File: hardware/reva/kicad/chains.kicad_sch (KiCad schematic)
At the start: 41 parts, among them SW1 REC_A, SW2 REC_B, SW3 MODBTN, SW4 SHIFTBTN

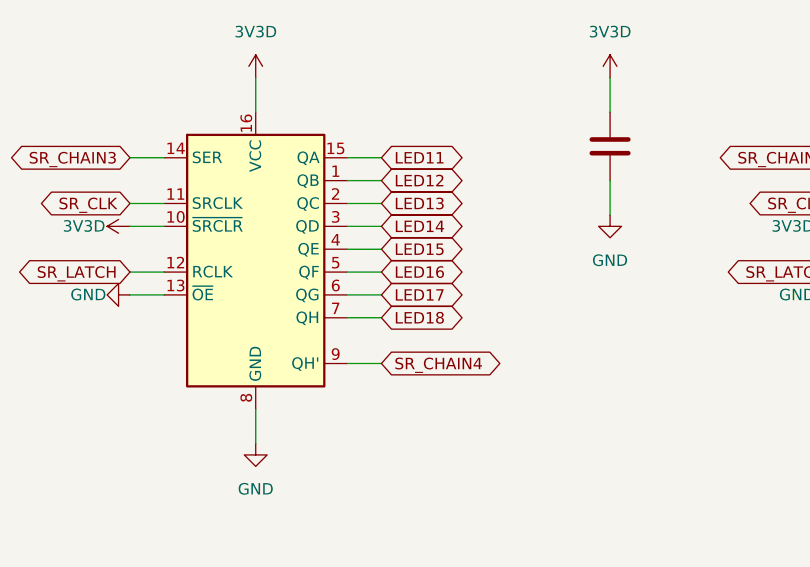
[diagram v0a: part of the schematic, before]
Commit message: feat(reva): 15 LED nets on the 595 chain, four more spare outputs
Spec 2026-10-07 section 5: 15 lamps (LED0..LED14), 73 pots. U_SR4 keeps
LED11..LED14 and gains SR_SPARE8..11, marked no-connect (four more test
points would wrap the chains sheet past the A3 title block). BOMs, review
sheet and the leds / mux sheets regenerated with hardware/reva/build.py.

Co-Authored-By: HAL 9000 <293417720+bea-ton-k@users.noreply.github.com>
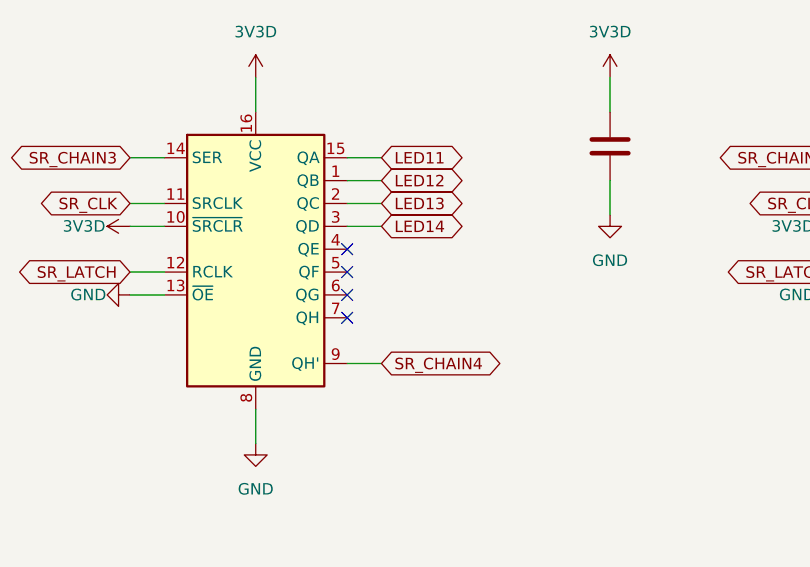
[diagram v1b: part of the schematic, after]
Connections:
- net LED15: no longer names the net of U_SR4.4 (QE)
- net LED16: no longer names the net of U_SR4.5 (QF)
- net LED17: no longer names the net of U_SR4.6 (QG)
- net LED18: no longer names the net of U_SR4.7 (QH)
- no-connect marks 18 -> 22
